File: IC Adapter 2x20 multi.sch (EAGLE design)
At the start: 12 parts, among them IC2 LTC6804IG-1#PBF, IC3 LTC6804IG-1#PBF, IC4 LTC6804IG-1#PBF

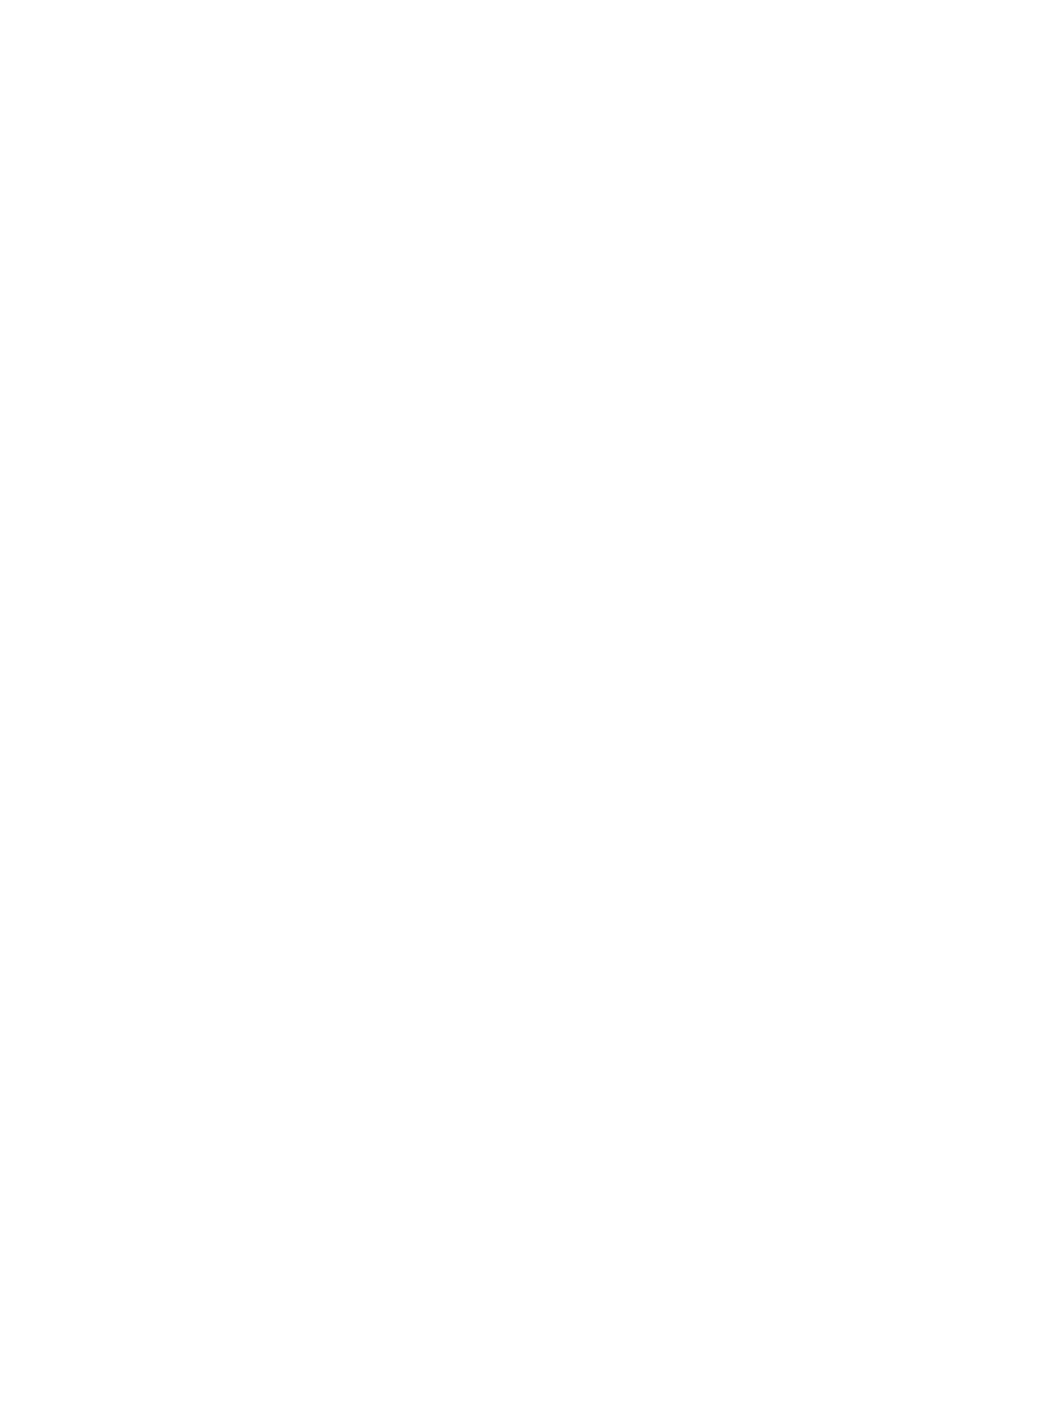
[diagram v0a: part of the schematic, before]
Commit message: multi made to 4x boards
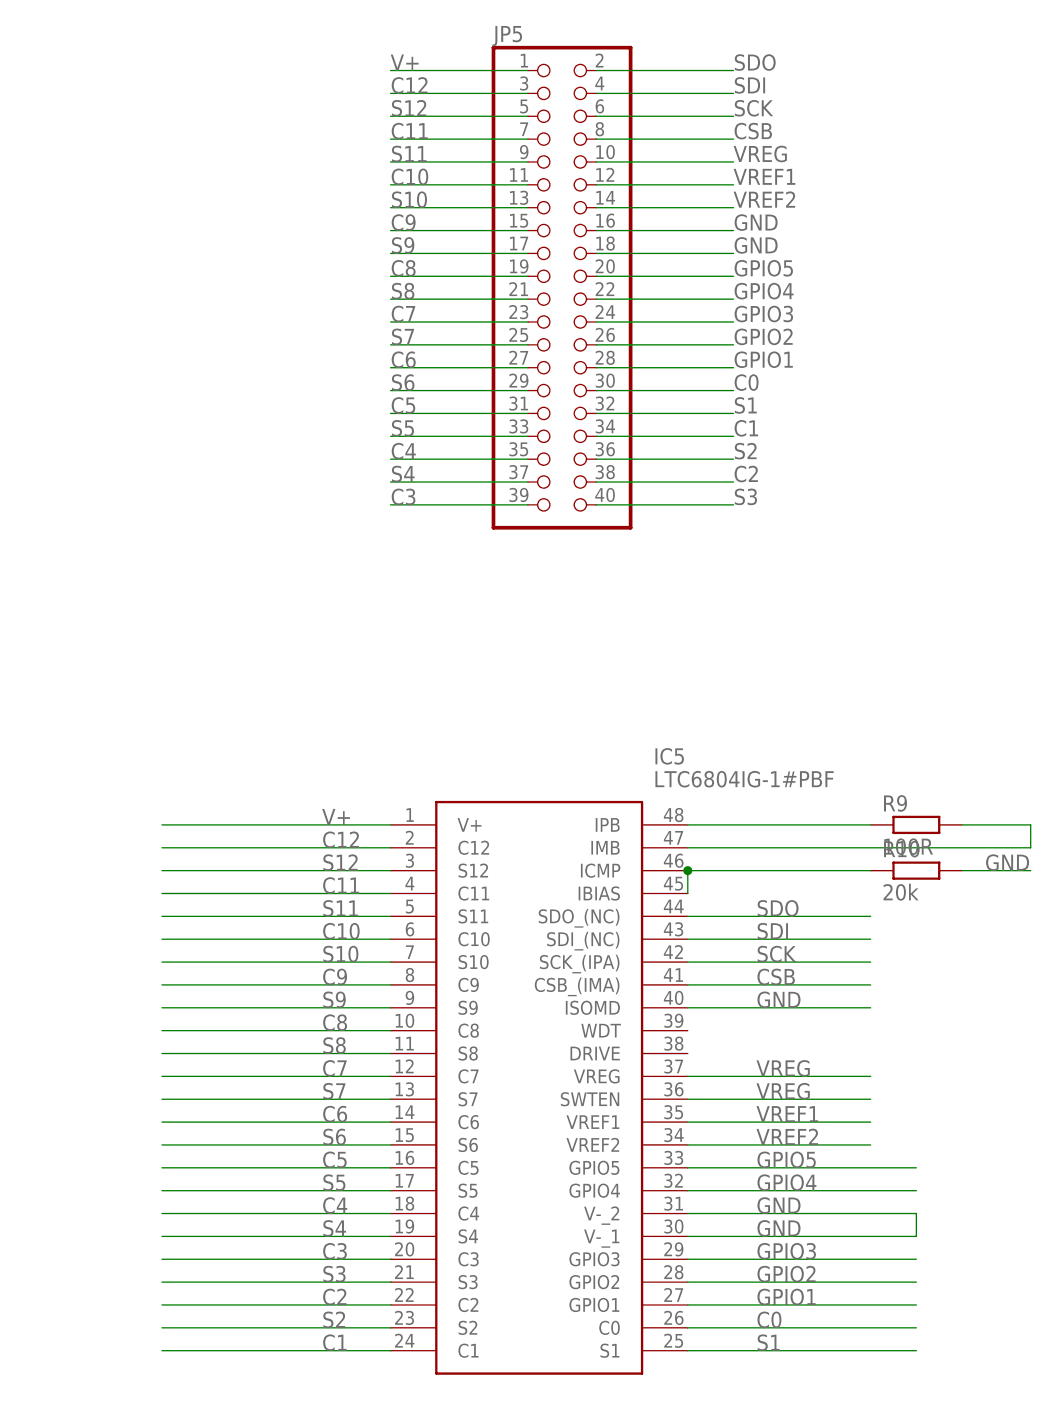
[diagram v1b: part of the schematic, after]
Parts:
- added IC5: LTC6804IG-1#PBF, SamacSys_Parts:LTC6804IG-1#PBF
- added JP5: (no value), pinhead:PINHD-2X20
- added R10: 20k, rcl:R-EU_R0805
- added R9: 100R, rcl:R-EU_R0805
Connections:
- new net ICMP4: IC5.IBIAS, IC5.ICMP, R10.1
- new net N$10: IC5.IMB, R9.2
- new net N$9: IC5.IPB, R9.1
- net C0: now also IC5.C0, JP5.30
- net C1: now also IC5.C1, JP5.34
- net C10: now also IC5.C10, JP5.11
- net C11: now also IC5.C11, JP5.7
- net C12: now also IC5.C12, JP5.3
- net C2: now also IC5.C2, JP5.38
- net C3: now also IC5.C3, JP5.39
- net C4: now also IC5.C4, JP5.35
- net C5: now also IC5.C5, JP5.31
- net C6: now also IC5.C6, JP5.27
- net C7: now also IC5.C7, JP5.23
- net C8: now also IC5.C8, JP5.19
- net C9: now also IC5.C9, JP5.15
- net CSB: now also IC5.CSB_(IMA), JP5.8
- net GND: now also IC5.ISOMD, IC5.V-_1, IC5.V-_2, JP5.16, JP5.18, R10.2
- net GPIO1: now also IC5.GPIO1, JP5.28
- net GPIO2: now also IC5.GPIO2, JP5.26
- net GPIO3: now also IC5.GPIO3, JP5.24
- net GPIO4: now also IC5.GPIO4, JP5.22
- net GPIO5: now also IC5.GPIO5, JP5.20
- net S1: now also IC5.S1, JP5.32
- net S10: now also IC5.S10, JP5.13
- net S11: now also IC5.S11, JP5.9
- net S12: now also IC5.S12, JP5.5
- net S2: now also IC5.S2, JP5.36
- net S3: now also IC5.S3, JP5.40
- net S4: now also IC5.S4, JP5.37
- net S5: now also IC5.S5, JP5.33
- net S6: now also IC5.S6, JP5.29
- net S7: now also IC5.S7, JP5.25
- net S8: now also IC5.S8, JP5.21
- net S9: now also IC5.S9, JP5.17
- net SCK: now also IC5.SCK_(IPA), JP5.6
- net SDI: now also IC5.SDI_(NC), JP5.4
- net SDO: now also IC5.SDO_(NC), JP5.2
- net V+: now also IC5.V+, JP5.1
- net VREF1: now also IC5.VREF1, JP5.12
- net VREF2: now also IC5.VREF2, JP5.14
- net VREG: now also IC5.SWTEN, IC5.VREG, JP5.10
